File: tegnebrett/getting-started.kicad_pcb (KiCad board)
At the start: 2 copper layers, 116 parts, among them J1 FH12-45S-0.5SH55, J2 FH12-6S-1SH55, J3 Conn_ST_STDC14, J4 DA15_Socket, J5 MCU_Header_Pin, J6 FPGA_Header_Pin, J8 USB-A1HSW6, U1 XC7A100T-2FTG256I, U2 Oscillator 100MHz, U3 TPS54294PWP1, U4 TPS54294PWP2, U5 STM32U5G7VJTxQ, U6 VGA Transceiver, U7 VGA Transciever, U8 IS66WVH16M8DBLL-100B1LI1, Y1 48MHz

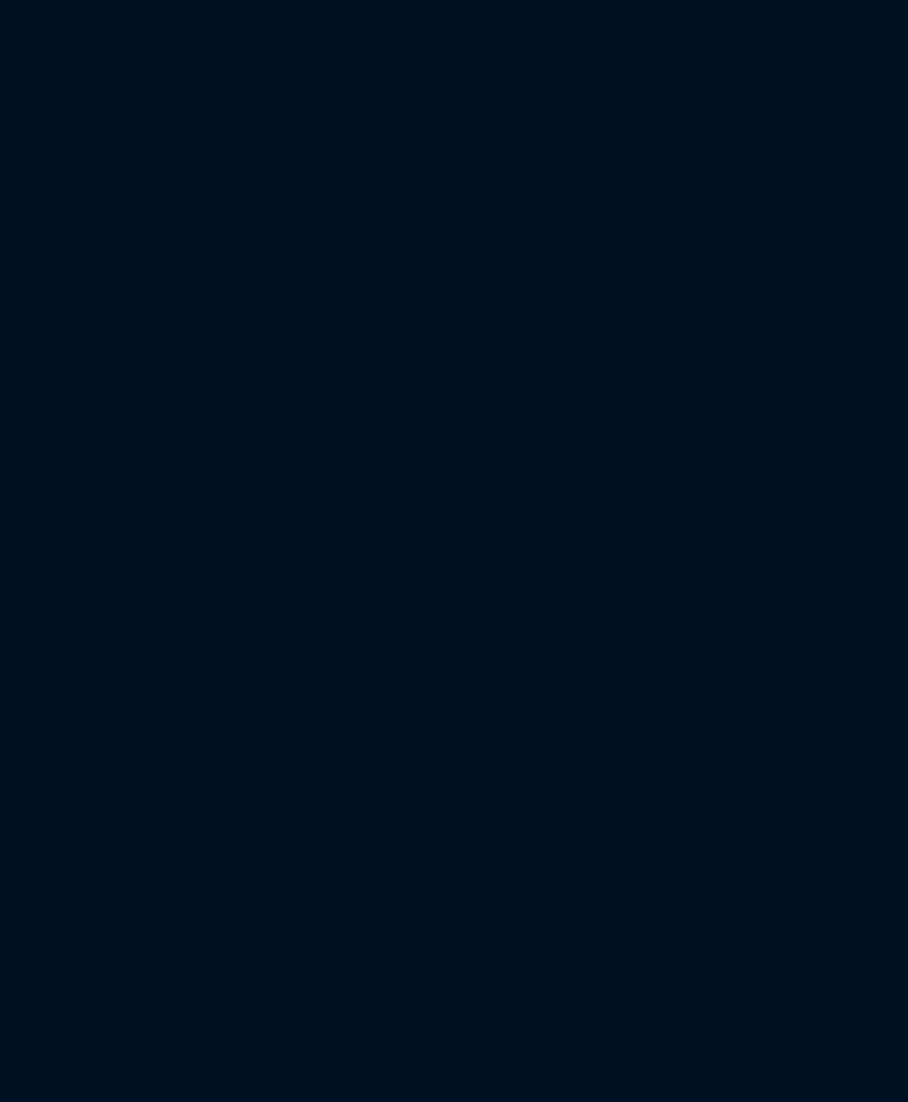
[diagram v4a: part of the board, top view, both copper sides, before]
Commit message: feat: import resistors to PCB
We're still lacking the resistors to the LEDs, we don't know what values
those should have.
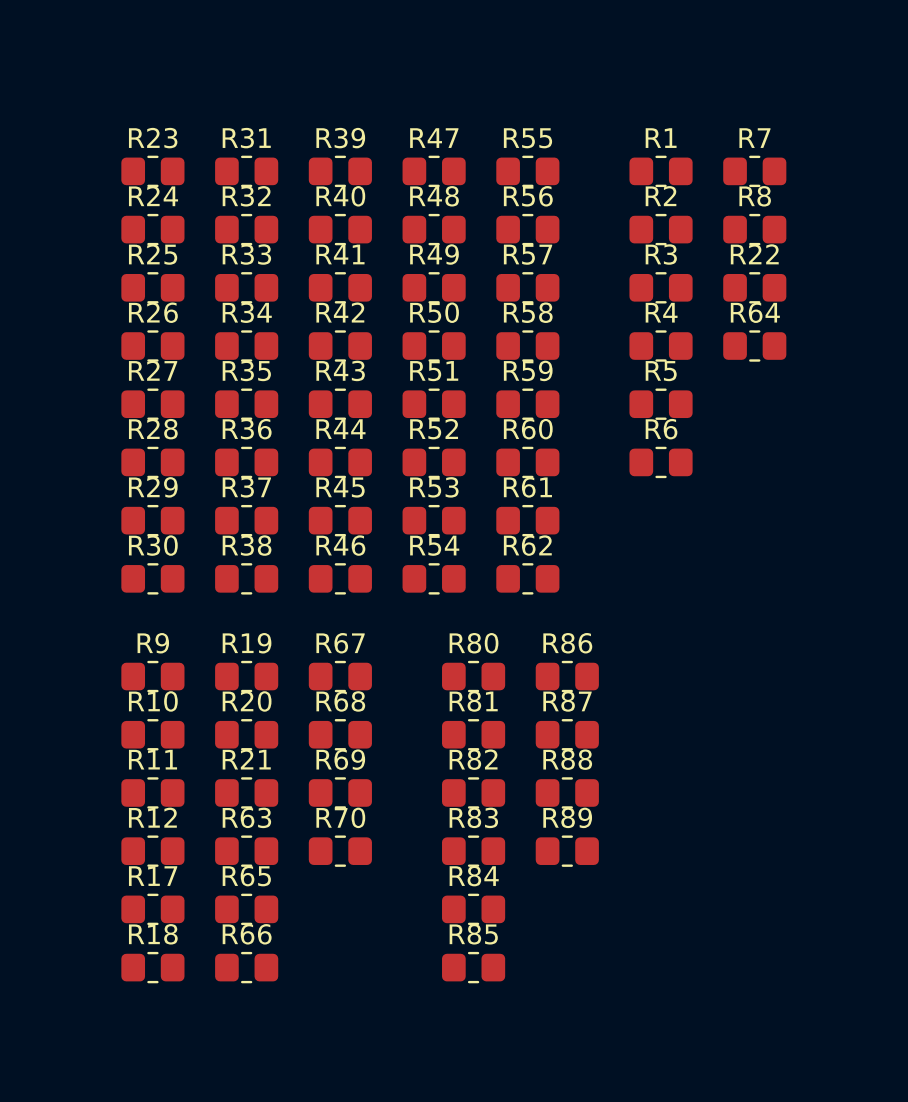
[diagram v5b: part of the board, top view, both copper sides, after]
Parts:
- added R1: 10k, Resistor_SMD:R_0805_2012Metric_Pad1.20x1.40mm_HandSolder, F.Cu at (144.5, 58.1)
- added R10: 47, Resistor_SMD:R_0805_2012Metric_Pad1.20x1.40mm_HandSolder, F.Cu at (118.8, 86.7)
- added R11: 47, Resistor_SMD:R_0805_2012Metric_Pad1.20x1.40mm_HandSolder, F.Cu at (118.8, 89.7)
- added R12: 47, Resistor_SMD:R_0805_2012Metric_Pad1.20x1.40mm_HandSolder, F.Cu at (118.8, 92.6)
- added R17: 4.7k, Resistor_SMD:R_0805_2012Metric_Pad1.20x1.40mm_HandSolder, F.Cu at (118.8, 95.5)
- added R18: 10k, Resistor_SMD:R_0805_2012Metric_Pad1.20x1.40mm_HandSolder, F.Cu at (118.8, 98.5)
- added R19: 4.7k, Resistor_SMD:R_0805_2012Metric_Pad1.20x1.40mm_HandSolder, F.Cu at (123.5, 83.8)
- added R2: 10k, Resistor_SMD:R_0805_2012Metric_Pad1.20x1.40mm_HandSolder, F.Cu at (144.5, 61.1)
- added R20: 4.7k, Resistor_SMD:R_0805_2012Metric_Pad1.20x1.40mm_HandSolder, F.Cu at (123.5, 86.7)
- added R21: 4.7k, Resistor_SMD:R_0805_2012Metric_Pad1.20x1.40mm_HandSolder, F.Cu at (123.5, 89.7)
- added R22: 4.7k, Resistor_SMD:R_0805_2012Metric_Pad1.20x1.40mm_HandSolder, F.Cu at (149.2, 64.0)
- added R23: 100K, Resistor_SMD:R_0805_2012Metric_Pad1.20x1.40mm_HandSolder, F.Cu at (118.8, 58.1)
- added R24: 100K, Resistor_SMD:R_0805_2012Metric_Pad1.20x1.40mm_HandSolder, F.Cu at (118.8, 61.1)
- added R25: 100K, Resistor_SMD:R_0805_2012Metric_Pad1.20x1.40mm_HandSolder, F.Cu at (118.8, 64.0)
- added R26: 100K, Resistor_SMD:R_0805_2012Metric_Pad1.20x1.40mm_HandSolder, F.Cu at (118.8, 67.0)
- added R27: 100K, Resistor_SMD:R_0805_2012Metric_Pad1.20x1.40mm_HandSolder, F.Cu at (118.8, 70.0)
- added R28: 100K, Resistor_SMD:R_0805_2012Metric_Pad1.20x1.40mm_HandSolder, F.Cu at (118.8, 72.9)
- added R29: 100K, Resistor_SMD:R_0805_2012Metric_Pad1.20x1.40mm_HandSolder, F.Cu at (118.8, 75.8)
- added R3: 330, Resistor_SMD:R_0805_2012Metric_Pad1.20x1.40mm_HandSolder, F.Cu at (144.5, 64.0)
- added R30: 100K, Resistor_SMD:R_0805_2012Metric_Pad1.20x1.40mm_HandSolder, F.Cu at (118.8, 78.8)
- added R31: 100K, Resistor_SMD:R_0805_2012Metric_Pad1.20x1.40mm_HandSolder, F.Cu at (123.5, 58.1)
- added R32: 100K, Resistor_SMD:R_0805_2012Metric_Pad1.20x1.40mm_HandSolder, F.Cu at (123.5, 61.1)
- added R33: 100K, Resistor_SMD:R_0805_2012Metric_Pad1.20x1.40mm_HandSolder, F.Cu at (123.5, 64.0)
- added R34: 100K, Resistor_SMD:R_0805_2012Metric_Pad1.20x1.40mm_HandSolder, F.Cu at (123.5, 67.0)
- added R35: 100K, Resistor_SMD:R_0805_2012Metric_Pad1.20x1.40mm_HandSolder, F.Cu at (123.5, 70.0)
- added R36: 100K, Resistor_SMD:R_0805_2012Metric_Pad1.20x1.40mm_HandSolder, F.Cu at (123.5, 72.9)
- added R37: 536, Resistor_SMD:R_0805_2012Metric_Pad1.20x1.40mm_HandSolder, F.Cu at (123.5, 75.8)
- added R38: 536, Resistor_SMD:R_0805_2012Metric_Pad1.20x1.40mm_HandSolder, F.Cu at (123.5, 78.8)
- added R39: 536, Resistor_SMD:R_0805_2012Metric_Pad1.20x1.40mm_HandSolder, F.Cu at (128.2, 58.1)
- added R4: 4.7k, Resistor_SMD:R_0805_2012Metric_Pad1.20x1.40mm_HandSolder, F.Cu at (144.5, 67.0)
- added R40: 536, Resistor_SMD:R_0805_2012Metric_Pad1.20x1.40mm_HandSolder, F.Cu at (128.2, 61.1)
- added R41: 536, Resistor_SMD:R_0805_2012Metric_Pad1.20x1.40mm_HandSolder, F.Cu at (128.2, 64.0)
- added R42: 536, Resistor_SMD:R_0805_2012Metric_Pad1.20x1.40mm_HandSolder, F.Cu at (128.2, 67.0)
- added R43: 536, Resistor_SMD:R_0805_2012Metric_Pad1.20x1.40mm_HandSolder, F.Cu at (128.2, 70.0)
- added R44: 536, Resistor_SMD:R_0805_2012Metric_Pad1.20x1.40mm_HandSolder, F.Cu at (128.2, 72.9)
- added R45: 270, Resistor_SMD:R_0805_2012Metric_Pad1.20x1.40mm_HandSolder, F.Cu at (128.2, 75.8)
- added R46: 270, Resistor_SMD:R_0805_2012Metric_Pad1.20x1.40mm_HandSolder, F.Cu at (128.2, 78.8)
- added R47: 270, Resistor_SMD:R_0805_2012Metric_Pad1.20x1.40mm_HandSolder, F.Cu at (133.0, 58.1)
- added R48: 536, Resistor_SMD:R_0805_2012Metric_Pad1.20x1.40mm_HandSolder, F.Cu at (133.0, 61.1)
- added R49: 270, Resistor_SMD:R_0805_2012Metric_Pad1.20x1.40mm_HandSolder, F.Cu at (133.0, 64.0)
- added R5: 4.7k, Resistor_SMD:R_0805_2012Metric_Pad1.20x1.40mm_HandSolder, F.Cu at (144.5, 70.0)
- added R50: 270, Resistor_SMD:R_0805_2012Metric_Pad1.20x1.40mm_HandSolder, F.Cu at (133.0, 67.0)
- added R51: 270, Resistor_SMD:R_0805_2012Metric_Pad1.20x1.40mm_HandSolder, F.Cu at (133.0, 70.0)
- added R52: 536, Resistor_SMD:R_0805_2012Metric_Pad1.20x1.40mm_HandSolder, F.Cu at (133.0, 72.9)
- added R53: 536, Resistor_SMD:R_0805_2012Metric_Pad1.20x1.40mm_HandSolder, F.Cu at (133.0, 75.8)
- added R54: 536, Resistor_SMD:R_0805_2012Metric_Pad1.20x1.40mm_HandSolder, F.Cu at (133.0, 78.8)
- added R55: 536, Resistor_SMD:R_0805_2012Metric_Pad1.20x1.40mm_HandSolder, F.Cu at (137.8, 58.1)
- added R56: 536, Resistor_SMD:R_0805_2012Metric_Pad1.20x1.40mm_HandSolder, F.Cu at (137.8, 61.1)
- added R57: 270, Resistor_SMD:R_0805_2012Metric_Pad1.20x1.40mm_HandSolder, F.Cu at (137.8, 64.0)
- added R58: 270, Resistor_SMD:R_0805_2012Metric_Pad1.20x1.40mm_HandSolder, F.Cu at (137.8, 67.0)
- added R59: 270, Resistor_SMD:R_0805_2012Metric_Pad1.20x1.40mm_HandSolder, F.Cu at (137.8, 70.0)
- added R6: 4.7k, Resistor_SMD:R_0805_2012Metric_Pad1.20x1.40mm_HandSolder, F.Cu at (144.5, 72.9)
- added R60: 536, Resistor_SMD:R_0805_2012Metric_Pad1.20x1.40mm_HandSolder, F.Cu at (137.8, 72.9)
- added R61: 100, Resistor_SMD:R_0805_2012Metric_Pad1.20x1.40mm_HandSolder, F.Cu at (137.8, 75.8)
- added R62: 100, Resistor_SMD:R_0805_2012Metric_Pad1.20x1.40mm_HandSolder, F.Cu at (137.8, 78.8)
- added R63: 4.7k, Resistor_SMD:R_0805_2012Metric_Pad1.20x1.40mm_HandSolder, F.Cu at (123.5, 92.6)
- added R64: 10K, Resistor_SMD:R_0805_2012Metric_Pad1.20x1.40mm_HandSolder, F.Cu at (149.2, 67.0)
- added R65: 4.7k, Resistor_SMD:R_0805_2012Metric_Pad1.20x1.40mm_HandSolder, F.Cu at (123.5, 95.5)
- added R66: 4.7k, Resistor_SMD:R_0805_2012Metric_Pad1.20x1.40mm_HandSolder, F.Cu at (123.5, 98.5)
- added R67: 4.7k, Resistor_SMD:R_0805_2012Metric_Pad1.20x1.40mm_HandSolder, F.Cu at (128.2, 83.8)
- added R68: 4.7k, Resistor_SMD:R_0805_2012Metric_Pad1.20x1.40mm_HandSolder, F.Cu at (128.2, 86.7)
- added R69: 4.7k, Resistor_SMD:R_0805_2012Metric_Pad1.20x1.40mm_HandSolder, F.Cu at (128.2, 89.7)
- added R7: 2.4k, Resistor_SMD:R_0805_2012Metric_Pad1.20x1.40mm_HandSolder, F.Cu at (149.2, 58.1)
- added R70: 4.7k, Resistor_SMD:R_0805_2012Metric_Pad1.20x1.40mm_HandSolder, F.Cu at (128.2, 92.6)
- added R8: 4.7k, Resistor_SMD:R_0805_2012Metric_Pad1.20x1.40mm_HandSolder, F.Cu at (149.2, 61.1)
- added R80: 6.81k, Resistor_SMD:R_0805_2012Metric_Pad1.20x1.40mm_HandSolder, F.Cu at (135.0, 83.8)
- added R81: 22.1k, Resistor_SMD:R_0805_2012Metric_Pad1.20x1.40mm_HandSolder, F.Cu at (135.0, 86.7)
- added R82: 100k, Resistor_SMD:R_0805_2012Metric_Pad1.20x1.40mm_HandSolder, F.Cu at (135.0, 89.7)
- added R83: 30.1k, Resistor_SMD:R_0805_2012Metric_Pad1.20x1.40mm_HandSolder, F.Cu at (135.0, 92.6)
- added R84: 22.1k, Resistor_SMD:R_0805_2012Metric_Pad1.20x1.40mm_HandSolder, F.Cu at (135.0, 95.5)
- added R85: 100k, Resistor_SMD:R_0805_2012Metric_Pad1.20x1.40mm_HandSolder, F.Cu at (135.0, 98.5)
- added R86: 73.2k, Resistor_SMD:R_0805_2012Metric_Pad1.20x1.40mm_HandSolder, F.Cu at (139.8, 83.8)
- added R87: 22.1k, Resistor_SMD:R_0805_2012Metric_Pad1.20x1.40mm_HandSolder, F.Cu at (139.8, 86.7)
- added R88: 124k, Resistor_SMD:R_0805_2012Metric_Pad1.20x1.40mm_HandSolder, F.Cu at (139.8, 89.7)
- added R89: 22.1k, Resistor_SMD:R_0805_2012Metric_Pad1.20x1.40mm_HandSolder, F.Cu at (139.8, 92.6)
- added R9: 47, Resistor_SMD:R_0805_2012Metric_Pad1.20x1.40mm_HandSolder, F.Cu at (118.8, 83.8)

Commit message: feat: import FPGA_debug header pin and buttons to PCB
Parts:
- added J9: FPGA_debug1, Connector_PinHeader_2.54mm:PinHeader_2x07_P2.54mm_Vertical, F.Cu at (64.5, 32.4)
- added R13: 4.7k, Resistor_SMD:R_0805_2012Metric_Pad1.20x1.40mm_HandSolder, F.Cu at (154.0, 58.0)
- added R14: 4.7k, Resistor_SMD:R_0805_2012Metric_Pad1.20x1.40mm_HandSolder, F.Cu at (154.0, 62.5)
- added SW1: SW_Push, tegnebrett_modules:SW_PS1024ALRED, F.Cu at (240.5, 60.2)
- added SW2: SW_Push, tegnebrett_modules:SW_PS1024ALRED, F.Cu at (240.5, 71.8)
- added SW3: Undo, tegnebrett_modules:SW_KS11R23CQD, F.Cu at (255.5, 60.0)
- added SW4: Reset, tegnebrett_modules:SW_KS11R23CQD, F.Cu at (253.2, 75.2)
- added SW5: MCU_Button, tegnebrett_modules:SW_PS1024ALRED, F.Cu at (240.5, 83.3)
- added SW6: FPGA_Button, tegnebrett_modules:SW_PS1024ALRED, F.Cu at (272.0, 60.0)
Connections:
- U1 pad G12: unconnected-(U1A-IO_L19N_T3_A21_VREF_15-PadG12) -> Net-(U1A-IO_L19N_T3_A21_VREF_15)
- U5 pad 53: Net-(U5-PB14) -> unconnected-(U5-PB14-Pad53)
- U5 pad 54: Net-(U5-PB15) -> unconnected-(U5-PB15-Pad54)
- U5 pad 63: Net-(U5-PC6) -> unconnected-(U5-PC6-Pad63)
- U5 pad 64: Net-(U5-PC7) -> unconnected-(U5-PC7-Pad64)

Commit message: feat: sort components on PCB layout.
Done by Tormod Sørum Dynna
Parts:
- removed D2, D3, D4, D5, D6, D7, D8, D9: LED, tegnebrett_modules:LED_J-SERIES_3030_CRW-M
- removed R65, R66, R67, R68, R69, R70: 4.7k, Resistor_SMD:R_0805_2012Metric_Pad1.20x1.40mm_HandSolder
- J3: value Conn_ST_STDC14 -> MCU_DEBUG
- moved J4 237.6 mm to (28.2, 23.5)
- moved U6 200.8 mm to (41.0, 50.0), turned to 180 degrees
- moved U7 200.5 mm to (41.5, 59.0), turned to 180 degrees
- moved C47 169.9 mm to (101.0, 13.5)
- moved C74 168.0 mm to (248.5, 73.0)
- moved C90 165.4 mm to (51.0, 55.5)
- moved C88 163.8 mm to (51.0, 51.5)
- moved J6 162.5 mm to (196.0, 14.7)
- moved C101 162.4 mm to (9.57, 97.8)
- moved C50 161.3 mm to (106.0, 30.0)
- moved C49 161.3 mm to (106.0, 27.0)
- moved C51 161.3 mm to (106.1, 33.0)
- moved C89 160.2 mm to (55.5, 55.5)
- moved C20 159.5 mm to (9.56, 94.0)
- moved C87 158.6 mm to (55.5, 51.5)
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
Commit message: feat: update PCB from schematic.
Added a few new components, mainly the Power jack connector.
This update may also have removed some components which are no longer
used, I don't know for sure.
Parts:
- added D1: LED, tegnebrett_modules:LED_LTST-C193KGKT-5A_LTO-M, F.Cu at (123.6, 103.6)
- added D2: LED, tegnebrett_modules:LED_LTST-C193KGKT-5A_LTO-M, F.Cu at (135.7, 108.6)
- added D3: LED, tegnebrett_modules:LED_LTST-C193KGKT-5A_LTO-M, F.Cu at (135.7, 111.6)
- added D8: LED, tegnebrett_modules:LED_LTST-C193KGKT-5A_LTO-M, F.Cu at (128.4, 108.6)
- added D9: LED, tegnebrett_modules:LED_LTST-C193KGKT-5A_LTO-M, F.Cu at (128.4, 111.6)
- added J7: PJ-002A, tegnebrett_modules:CUI_PJ-002A, F.Cu at (123.7, 96.8)
- added R15: 270, Resistor_SMD:R_0805_2012Metric_Pad1.20x1.40mm_HandSolder, F.Cu at (128.5, 103.5)
- added R65: 4.7k, Resistor_SMD:R_0805_2012Metric_Pad1.20x1.40mm_HandSolder, F.Cu at (123.2, 108.5)
- added R72: 270, Resistor_SMD:R_0805_2012Metric_Pad1.20x1.40mm_HandSolder, F.Cu at (140.5, 108.5)
- added R73: 270, Resistor_SMD:R_0805_2012Metric_Pad1.20x1.40mm_HandSolder, F.Cu at (140.5, 111.5)
- added R78: 270, Resistor_SMD:R_0805_2012Metric_Pad1.20x1.40mm_HandSolder, F.Cu at (123.2, 111.5)
- added R79: 270, Resistor_SMD:R_0805_2012Metric_Pad1.20x1.40mm_HandSolder, F.Cu at (123.2, 114.5)
- J3: value MCU_DEBUG -> Conn_ST_STDC14
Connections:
- C14 pad 1: POWER_IN -> Net-(U4-EN1)
- C25 pad 1: POWER_IN -> Net-(U4-EN1)
- C30 pad 1: POWER_IN -> Net-(U4-EN1)
- C8 pad 1: POWER_IN -> Net-(U4-EN1)
- U1 pad G15: Net-(U1A-IO_L24N_T3_RS0_15) -> unconnected-(U1A-IO_L24N_T3_RS0_15-PadG15)
- U4 pad 1: POWER_IN -> Net-(U4-EN1)
- U4 pad 16: POWER_IN -> Net-(U4-EN1)
- U4 pad 5: POWER_IN -> Net-(U4-EN1)
- U5 pad 67: Net-(U5-PA8) -> unconnected-(U5-PA8-Pad67)
- U5 pad 68: Net-(U5-PA9) -> unconnected-(U5-PA9-Pad68)
- U5 pad 69: Net-(U5-PA10) -> unconnected-(U5-PA10-Pad69)
